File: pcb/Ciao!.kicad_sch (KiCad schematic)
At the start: 82 parts, among them SW1 SW_Push_45deg, SW10 SW_Push_45deg, SW11 SW_Push_45deg, SW12 SW_Push_45deg, SW13 SW_Push_45deg, SW14 SW_Push_45deg, SW15 SW_Push_45deg, SW16 SW_Push_45deg, SW17 SW_Push_45deg, SW18 SW_Push_45deg, SW19 SW_Push_45deg, SW2 SW_Push_45deg, SW20 SW_Push_45deg, SW21 SW_Push_45deg, SW22 SW_Push_45deg, SW23 SW_Push_45deg, SW24 SW_Push_45deg, SW25 SW_Push_45deg, SW26 SW_Push_45deg, SW27 SW_Push_45deg, SW28 SW_Push_45deg, SW29 SW_Push_45deg, SW3 SW_Push_45deg, SW30 SW_Push_45deg, SW31 SW_Push_45deg, SW32 SW_Push_45deg, SW33 SW_Push_45deg, SW34 SW_Push_45deg, SW35 SW_Push_45deg, SW36 SW_Push_45deg, SW37 SW_Push_45deg, SW4 SW_Push_45deg, SW5 SW_Push_45deg, SW6 SW_Push_45deg, SW7 SW_Push_45deg, SW8 SW_Push_45deg, SW9 SW_Push_45deg, U1 Seeeduino Xiao nRF52840 Plus

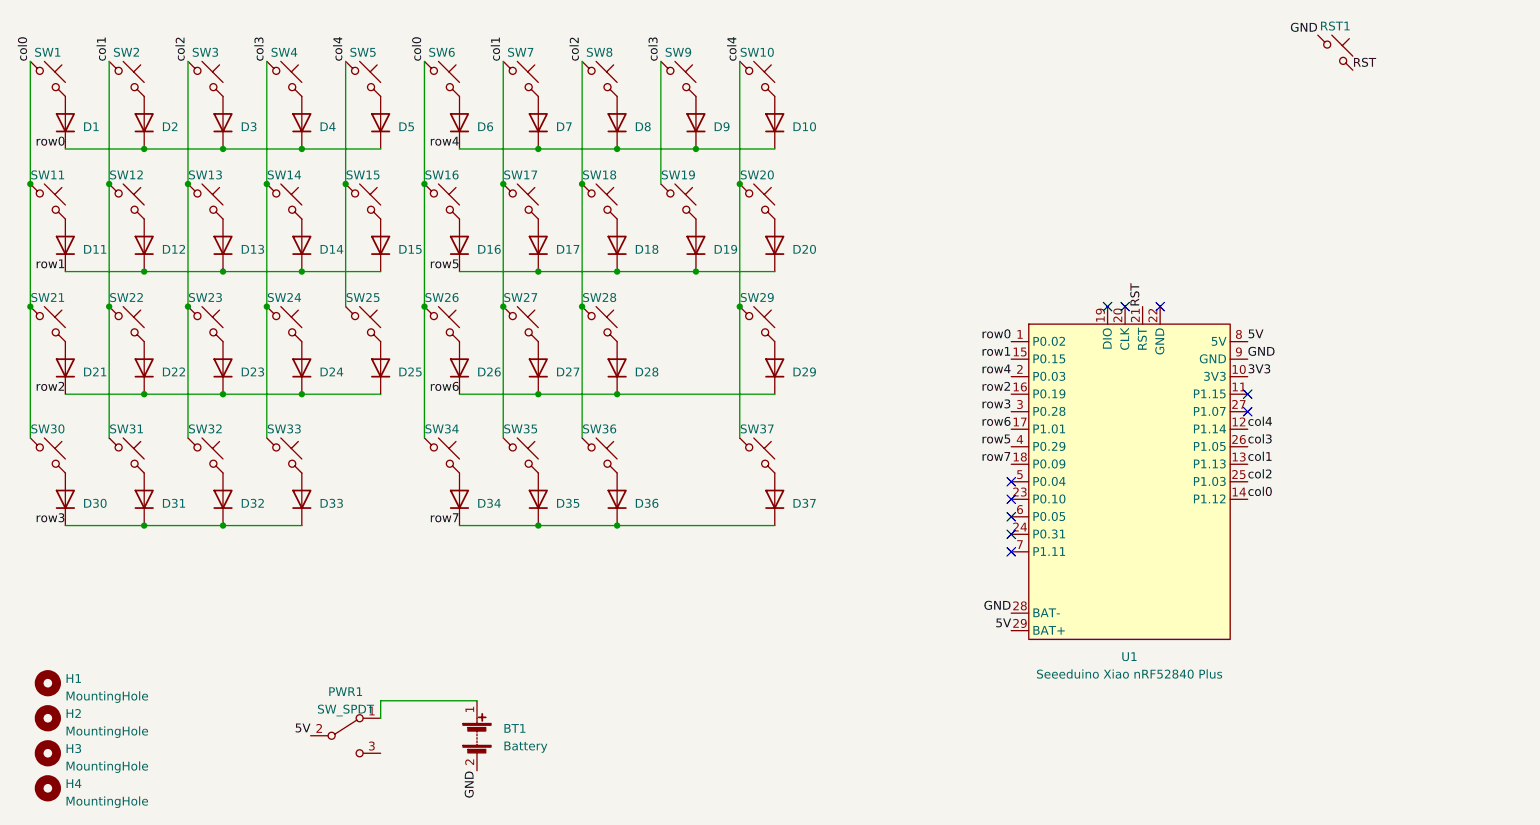
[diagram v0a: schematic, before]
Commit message: finished pcb, needs more cleanup
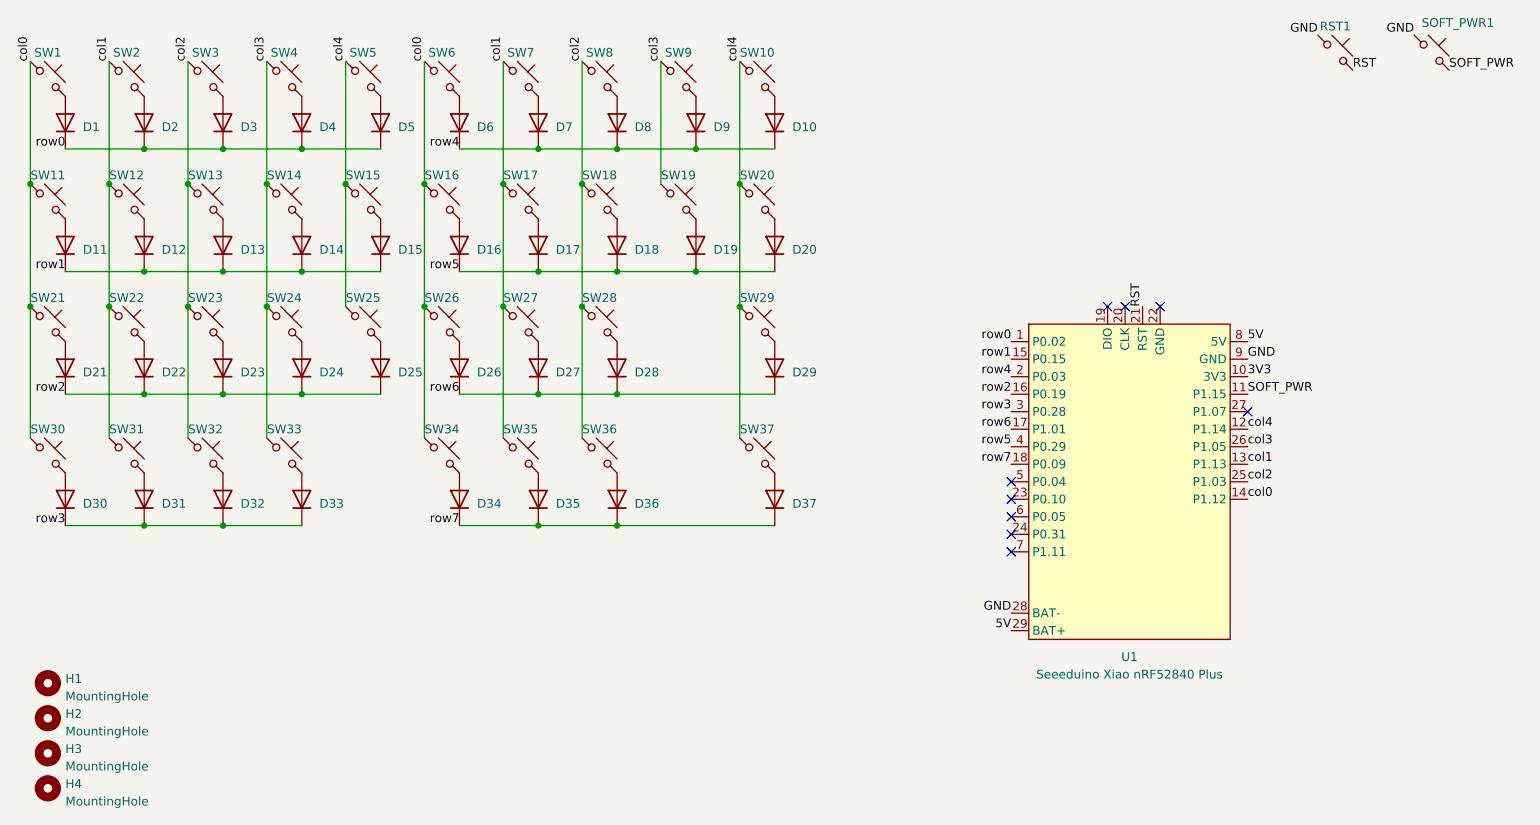
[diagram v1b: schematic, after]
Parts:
- removed BT1: Battery, chaz:3JST_BAT, symbol Device:Battery
- removed PWR1: SW_SPDT, 0-jasonhazel-footprints:SW_CuK_OS102011MA1QN1_SPDT_Angled, symbol Switch:SW_SPDT
- added SOFT_PWR1: SW_Push_45deg, chaz:SKHLLCA010, symbol Switch:SW_Push_45deg
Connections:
- net GND: now also SOFT_PWR1.1
- net SOFT_PWR: now reaches U1.11 (P1.15)
- net SOFT_PWR: now also SOFT_PWR1.2
- no-connect marks 10 -> 9
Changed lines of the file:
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@@
 	)
 	(no_connect
-		(at 200.66 73.66)
-	)
-	(no_connect
 		(at 166.37 88.9)
 	)
@@
 	(wire
 		(pts
-			(xy 88.9 118.11) (xy 74.93 118.11)
-		)
-		(stroke
-			(width 0)
-			(type default)
-		)
-	)
-	(wire
-		(pts
 			(xy 58.42 43.18) (xy 58.42 60.96)
 		)
@@
 	(wire
 		(pts
-			(xy 74.93 118.11) (xy 74.93 120.65)
-		)
-		(stroke
-			(width 0)
-			(type default)
-		)
-	)
-	(wire
-		(pts
 			(xy 40.64 55.88) (xy 52.07 55.88)
 		)
@@
 		)
 	)
-	(label "GND"
-		(at 88.9 128.27 270)
+	(label "SOFT_PWR"
+		(at 229.87 26.67 0)
 		(effects
 			(font
 				(size 1.27 1.27)
 			)
-			(justify right bottom)
+			(justify left bottom)
 		)
 	)
@@
 		)
 	)
+	(label "SOFT_PWR"
+		(at 200.66 73.66 0)
+		(effects
+			(font
+				(size 1.27 1.27)
+			)
+			(justify left bottom)
+		)
+	)
 	(label "row2"
 		(at 29.21 73.66 180)
@@
 		)
 	)
-	(label "5V"
-		(at 64.77 123.19 180)
-		(effects
-			(font
-				(size 1.27 1.27)
-			)
-			(justify right bottom)
-		)
-	)
 	(label "col1"
 		(at 35.56 25.4 90)
@@
 		)
 	)
+	(label "GND"
+		(at 224.79 21.59 180)
+		(effects
+			(font
+				(size 1.27 1.27)
+			)
+			(justify right bottom)
+		)
+	)
 	(label "col2"
 		(at 46.99 25.4 90)
@@
 	)
 	(symbol
-		(lib_id "Switch:SW_SPDT")
-		(at 69.85 123.19 0)
-		(unit 1)
-		(exclude_from_sim no)
-		(in_bom yes)
-		(on_board yes)
-		(dnp no)
-		(fields_autoplaced yes)
-		(property "Reference" "PWR1"
-			(at 69.85 116.84 0)
-			(effects
-				(font
-					(size 1.27 1.27)
-				)
-			)
-		)
-		(property "Value" "SW_SPDT"
-			(at 69.85 119.38 0)
-			(effects
-				(font
-					(size 1.27 1.27)
-				)
-			)
-		)
-		(property "Footprint" "0-jasonhazel-footprints:SW_CuK_OS102011MA1QN1_SPDT_Angled"
-			(at 69.85 123.19 0)
-			(effects
-				(font
-					(size 1.27 1.27)
-				)
-				(hide yes)
-			)
-		)
-		(property "Datasheet" "~"
-			(at 69.85 123.19 0)
-			(effects
-				(font
-					(size 1.27 1.27)
-				)
-				(hide yes)
-			)
-		)
-		(property "Description" ""
-			(at 69.85 123.19 0)
-			(effects
-				(font
-					(size 1.27 1.27)
-				)
-				(hide yes)
-			)
-		)
-		(pin "1"
-		)
-		(pin "2"
-		)
-		(pin "3"
-		)
-		(instances
-			(project "chaz"
-				(path "/42c73bb5-2111-43a9-aabb-3d391c8f2d68"
-					(reference "PWR1")
-					(unit 1)
-				)
-			)
-		)
-	)
-	(symbol
 		(lib_id "Diode:1N4148W")
 		(at 63.5 69.85 90)
@@
 	)
 	(symbol
+		(lib_id "Switch:SW_Push_45deg")
+		(at 227.33 24.13 0)
+		(unit 1)
+		(exclude_from_sim no)
+		(in_bom yes)
+		(on_board yes)
+		(dnp no)
+		(property "Reference" "SOFT_PWR1"
+			(at 231.14 19.812 0)
+			(effects
+				(font
+					(size 1.27 1.27)
+				)
+			)
+		)
+		(property "Value" "SW_Push_45deg"
+			(at 227.33 20.32 0)
+			(effects
+				(font
+					(size 1.27 1.27)
+				)
+				(hide yes)
+			)
+		)
+		(property "Footprint" "chaz:SKHLLCA010"
+			(at 227.33 24.13 0)
+			(effects
+				(font
+					(size 1.27 1.27)
+				)
+				(hide yes)
+			)
+		)
+		(property "Datasheet" "~"
+			(at 227.33 24.13 0)
+			(effects
+				(font
+					(size 1.27 1.27)
+				)
+				(hide yes)
+			)
+		)
+		(property "Description" ""
+			(at 227.33 24.13 0)
+			(effects
+				(font
+					(size 1.27 1.27)
+				)
+				(hide yes)
+			)
+		)
+		(pin "1"
+		)
+		(pin "2"
+		)
+		(instances
+			(project "Ciao!"
+				(path "/42c73bb5-2111-43a9-aabb-3d391c8f2d68"
+					(reference "SOFT_PWR1")
+					(unit 1)
+				)
+			)
+		)
+	)
+	(symbol
 		(lib_id "Mechanical:MountingHole")
 		(at 26.67 125.73 0)
@@
 					(unit 1)
 				)
-			)
-		)
-	)
-	(symbol
-		(lib_id "Device:Battery")
-		(at 88.9 123.19 0)
-		(unit 1)
-		(exclude_from_sim no)
-		(in_bom yes)
-		(on_board yes)
-		(dnp no)
-		(fields_autoplaced yes)
-		(property "Reference" "BT1"
-			(at 92.71 122.174 0)
-			(effects
-				(font
-					(size 1.27 1.27)
-				)
-				(justify left)
-			)
-		)
-		(property "Value" "Battery"
-			(at 92.71 124.714 0)
-			(effects
-				(font
-					(size 1.27 1.27)
-				)
-				(justify left)
-			)
-		)
-		(property "Footprint" "chaz:3JST_BAT"
-			(at 88.9 121.666 90)
-			(effects
-				(font
-					(size 1.27 1.27)
-				)
-				(hide yes)
-			)
-		)
-		(property "Datasheet" "~"
-			(at 88.9 121.666 90)
-			(effects
-				(font
-					(size 1.27 1.27)
-				)
-				(hide yes)
-			)
-		)
-		(property "Description" ""
-			(at 88.9 123.19 0)
-			(effects
-				(font
-					(size 1.27 1.27)
-				)
-				(hide yes)
-			)
-		)
-		(pin "1"
-		)
-		(pin "2"
-		)
-		(instances
-			(project "chaz"
-				(path "/42c73bb5-2111-43a9-aabb-3d391c8f2d68"
-					(reference "BT1")
-					(unit 1)
-				)
